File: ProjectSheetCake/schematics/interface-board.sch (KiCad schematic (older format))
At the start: 42 parts, among them P1 CONN_8, P2 CONN_6, P3 CONN_8, P4 CONN_6, P7 Y_X_SERVO, P8 A_Z_SERVO

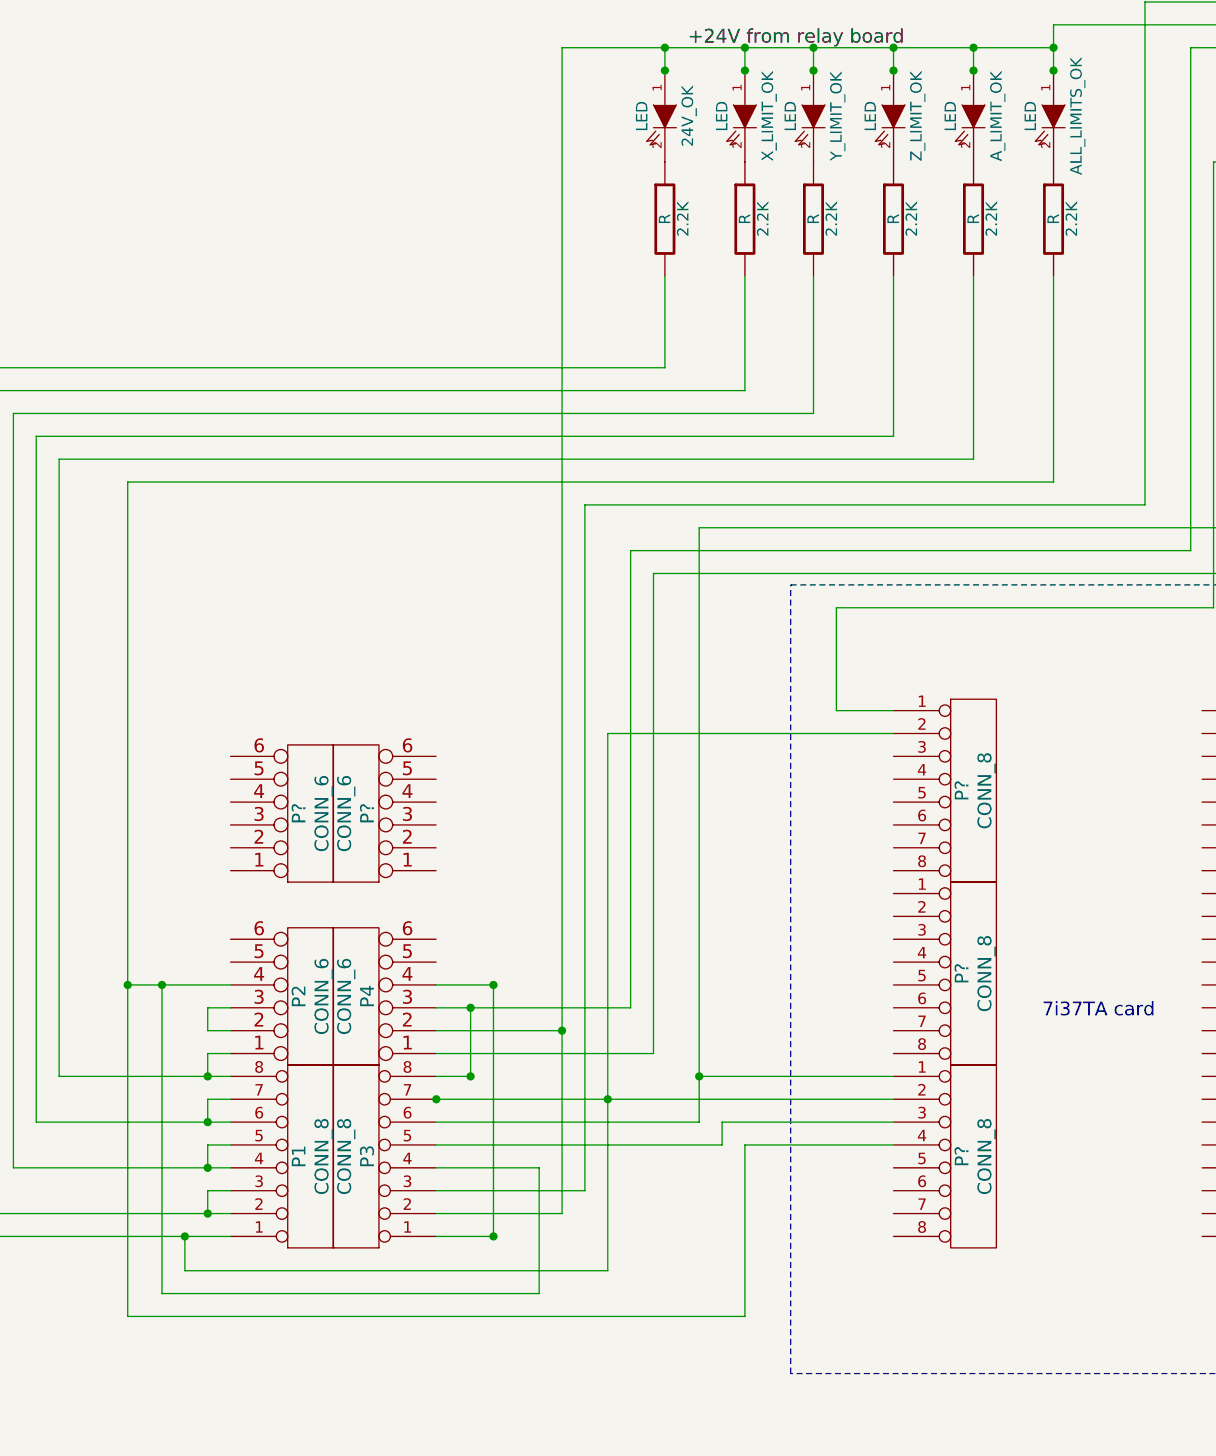
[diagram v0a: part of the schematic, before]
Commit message: added image for classic ladder program
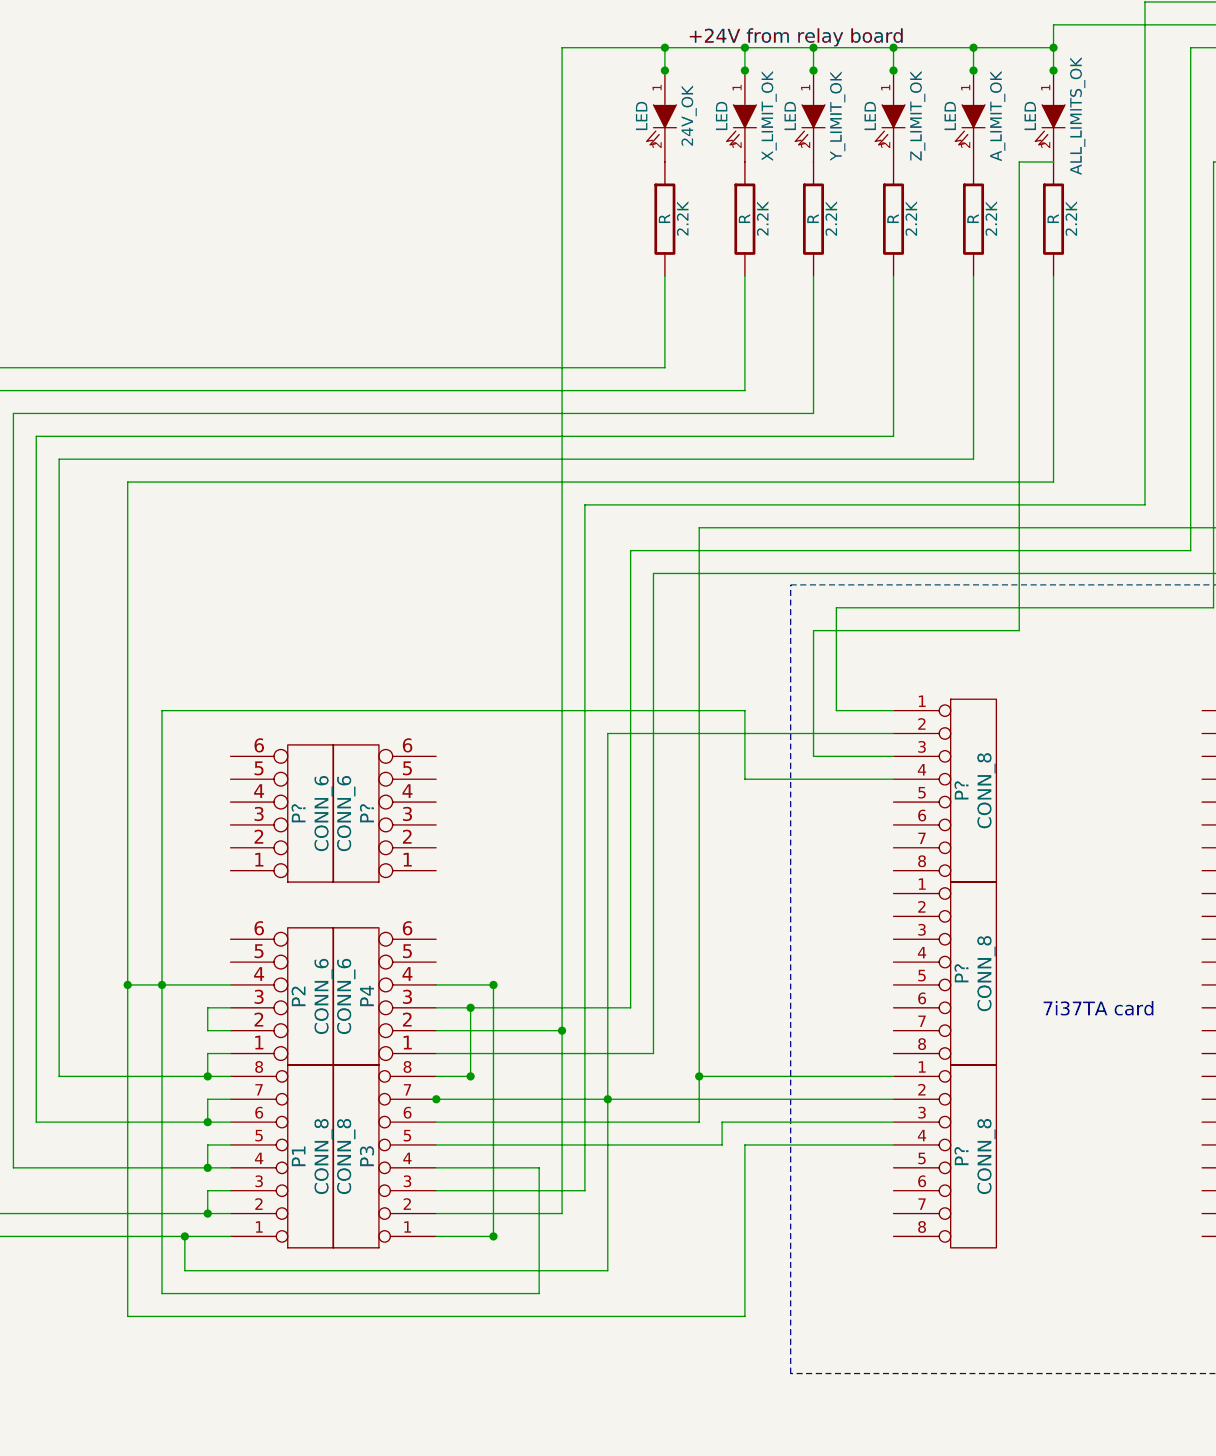
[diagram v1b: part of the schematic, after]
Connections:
- wire segments 247 -> 255
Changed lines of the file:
@@
-EESchema Schematic File Version 2  date 8/19/2011 10:26:13 PM
+EESchema Schematic File Version 2  date 8/25/2011 11:29:30 PM
 LIBS:power
 LIBS:device
@@
 LIBS:contrib
 LIBS:valves
+LIBS:interface-board-cache
 EELAYER 25  0
 EELAYER END
@@
 Sheet 1 1
 Title ""
-Date "20 aug 2011"
+Date "26 aug 2011"
 Rev ""
 Comp ""
@@
 Comment4 ""
 $EndDescr
+Wire Wire Line
+	4850 4450 4200 4450
+Wire Wire Line
+	4200 4450 4200 4150
+Wire Wire Line
+	1650 4150 4200 4150
+Wire Wire Line
+	1650 4150 1650 6700
 Wire Wire Line
 	16200 8600 10500 8600
@@
 Connection ~ 1650 5350
 Wire Wire Line
-	1650 5350 1650 6700
-Wire Wire Line
 	1650 6700 3300 6700
 Wire Wire Line
@@
 Wire Wire Line
 	10600 8500 16100 8500
+Wire Wire Line
+	5550 1750 5400 1750
+Wire Wire Line
+	5400 1750 5400 3800
+Wire Wire Line
+	5400 3800 4500 3800
+Wire Wire Line
+	4500 3800 4500 4350
+Wire Wire Line
+	4500 4350 4850 4350
 Text Notes 9400 5450 0    60   ~ 0
 7i33TA card

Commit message: updated schematics and images
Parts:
- 1-8, 17-24, 9-16: renamed from P?; value CONN_8 -> TB2
- 1-8, 17-24, 9-16: renamed from P?; value CONN_8 -> TB1
- 17-24: renamed from P?; value CONN_8 -> TB1; footprint (none) -> ~
- P1: value CONN_8 -> Limits
- P2: value CONN_6 -> More limits
- P3: value CONN_8 -> Relay board
- P4: value CONN_6 -> Estops/reset
- P5: renamed from P?; value CONN_6 -> Power supply
- P6: renamed from P?; value CONN_6 -> UNUSED
- renumbered P8 to P7, P7 to P8
